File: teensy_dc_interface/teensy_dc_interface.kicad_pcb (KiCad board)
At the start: 2 copper layers, 125 parts, among them J1 3.5mm_Mono_Switched_SymSmall_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, J2 3.5mm_Mono_Switched_SymSmall_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, J3 3.5mm_Mono_Switched_SymSmall_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, J4 3.5mm_Mono_Switched_SymSmall_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, J5 3.5mm_Mono_Switched_SymSmall_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, J6 3.5mm_Mono_Switched_SymSmall_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, J7 3.5mm_Mono_Switched_SymSmall_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, J8 3.5mm_Mono_Switched_SymSmall_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, U1 AK4458VN, U2 Teensy4.0, U3 AP65211A, U4 AP62200TWU-7, U5 NE5532, U6 NE5532, U7 NE5532, U8 NE5532

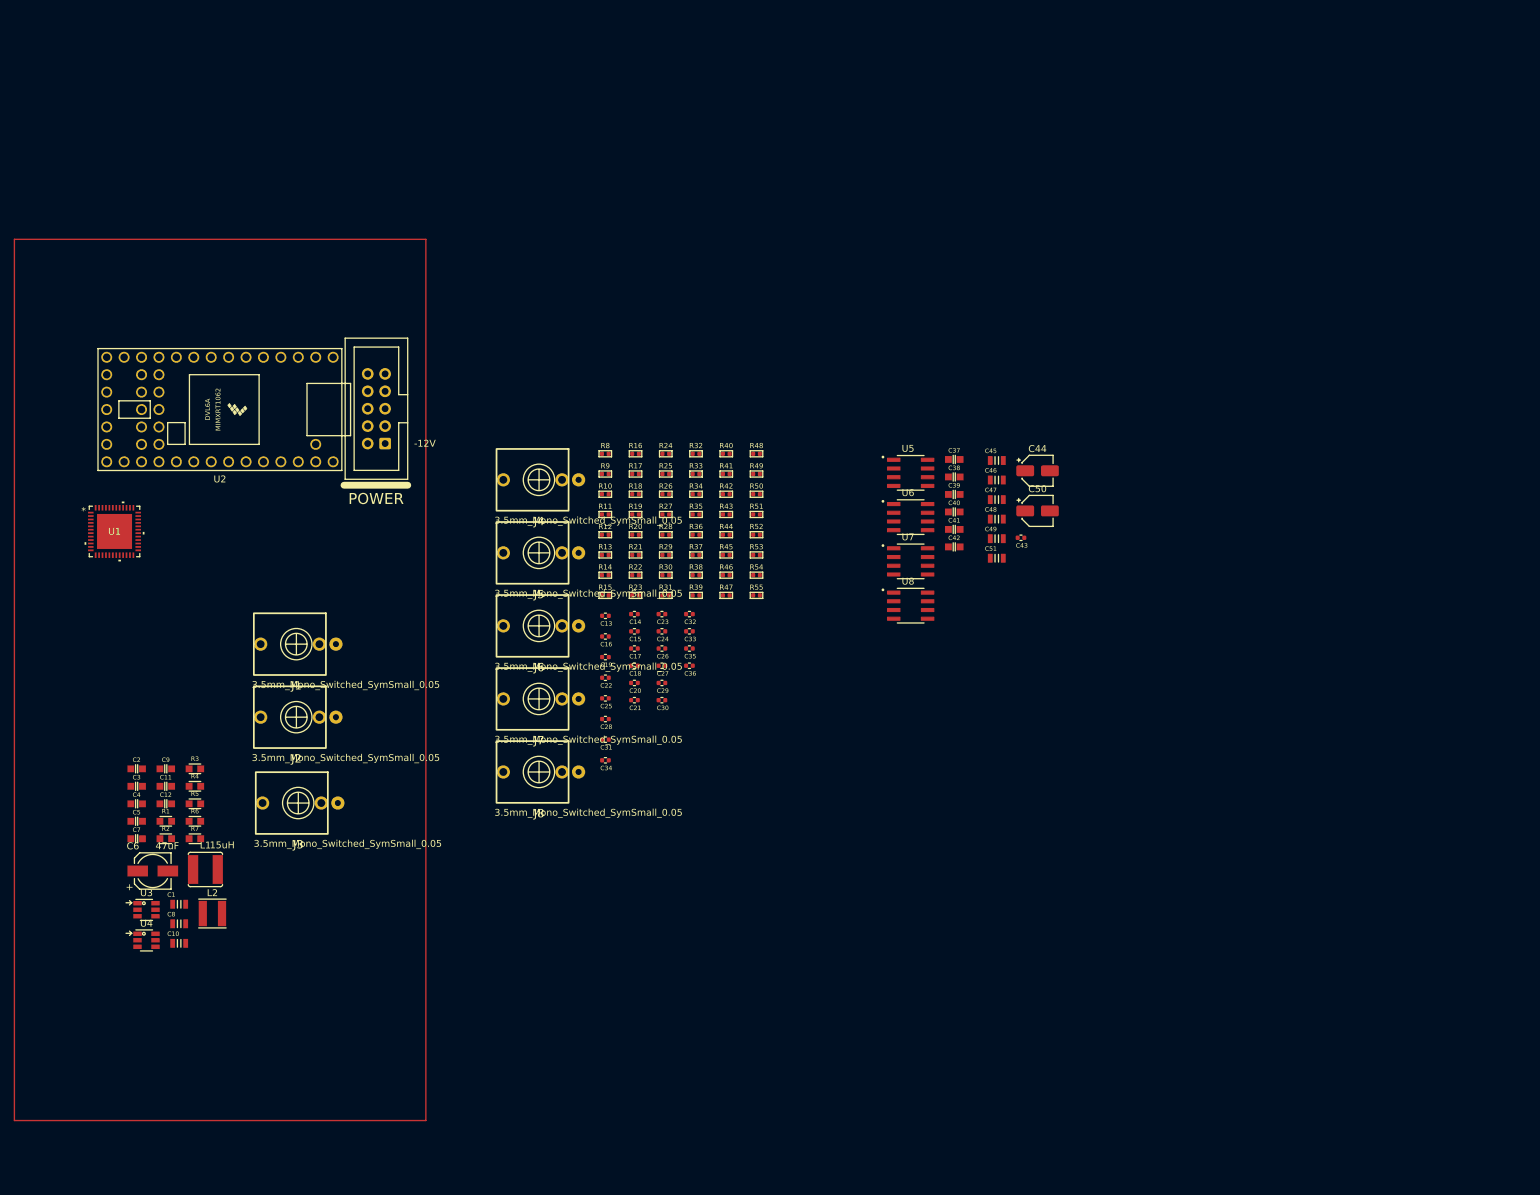
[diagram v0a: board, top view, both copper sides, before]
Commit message: teensy to dac connections
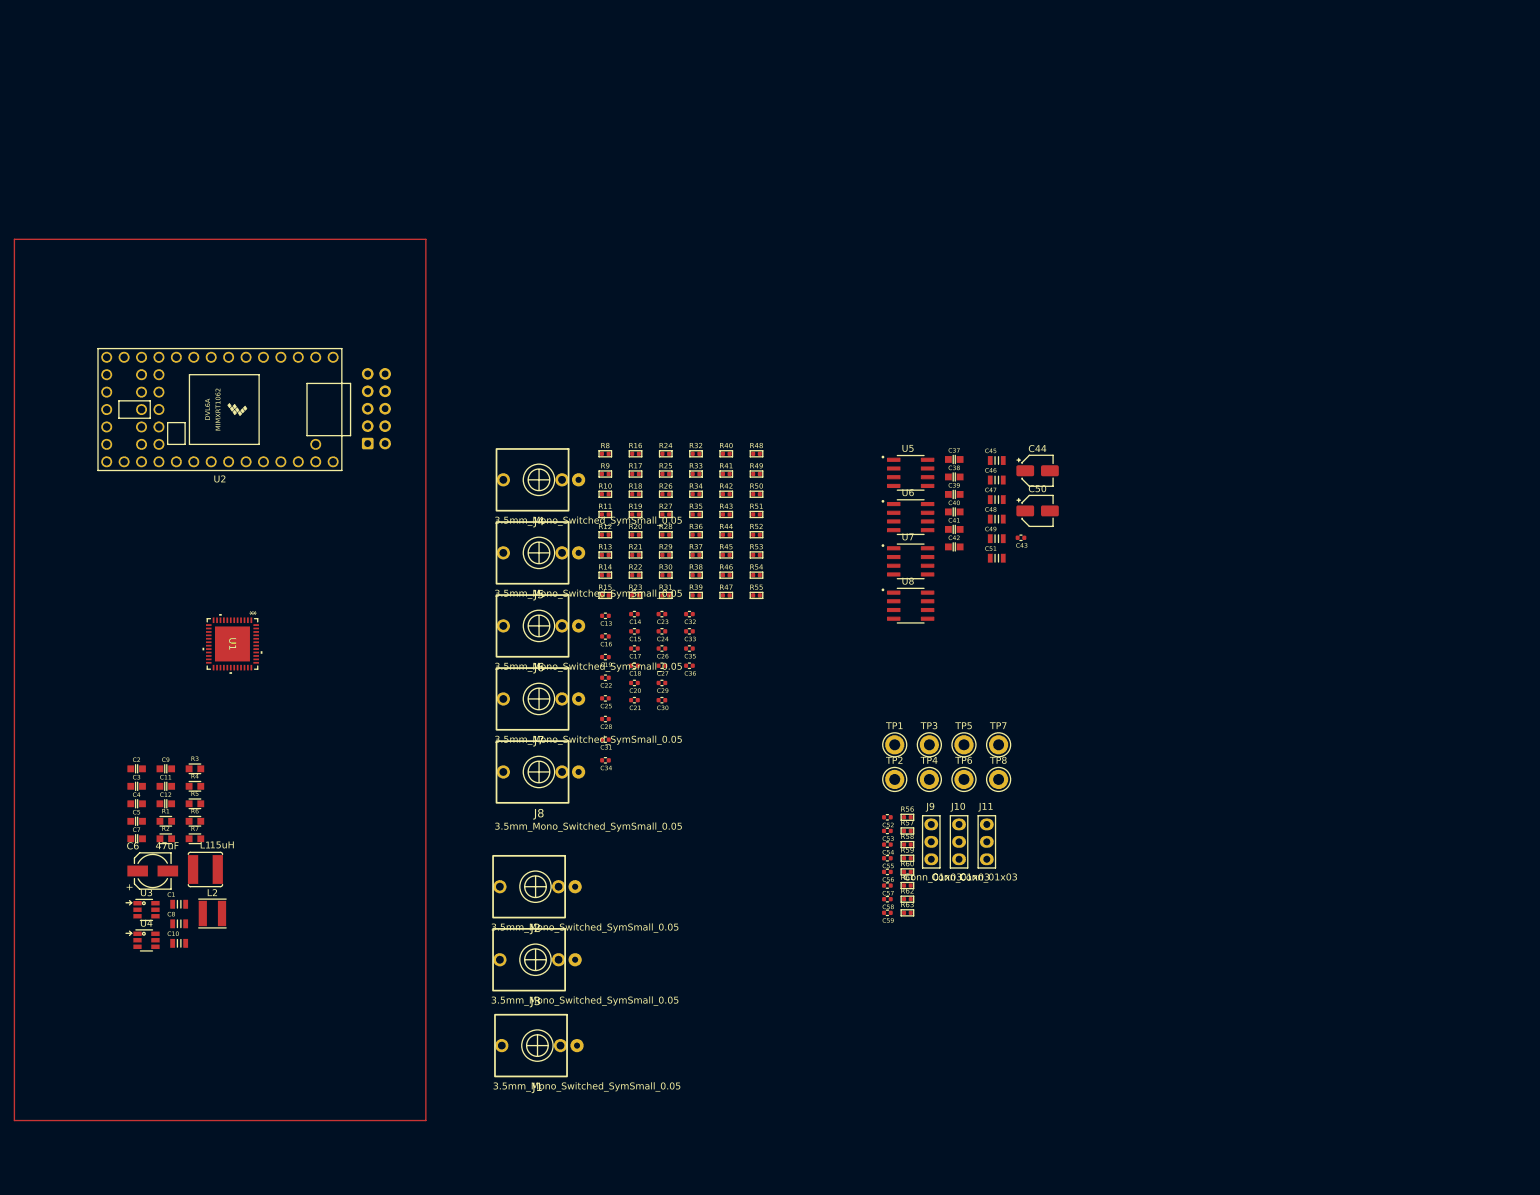
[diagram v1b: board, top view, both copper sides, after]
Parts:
- added C52: 220pF_0402_50V, 4ms_Capacitor:C_0402, F.Cu at (157.3, 104.3)
- added C53: 220pF_0402_50V, 4ms_Capacitor:C_0402, F.Cu at (157.3, 106.3)
- added C54: 220pF_0402_50V, 4ms_Capacitor:C_0402, F.Cu at (157.3, 108.3)
- added C55: 220pF_0402_50V, 4ms_Capacitor:C_0402, F.Cu at (157.3, 110.2)
- added C56: 220pF_0402_50V, 4ms_Capacitor:C_0402, F.Cu at (157.3, 112.2)
- added C57: 220pF_0402_50V, 4ms_Capacitor:C_0402, F.Cu at (157.3, 114.2)
- added C58: 220pF_0402_50V, 4ms_Capacitor:C_0402, F.Cu at (157.3, 116.2)
- added C59: 220pF_0402_50V, 4ms_Capacitor:C_0402, F.Cu at (157.3, 118.2)
- added J10: Conn_01x03, 4ms_Connector:Pins_1x03_2.54mm_TH, F.Cu at (167.8, 107.9)
- added J11: Conn_01x03, 4ms_Connector:Pins_1x03_2.54mm_TH, F.Cu at (171.8, 107.9)
- added J9: Conn_01x03, 4ms_Connector:Pins_1x03_2.54mm_TH, F.Cu at (163.7, 107.9)
- added R56: 10R_0402, 4ms_Resistor:R_0402, F.Cu at (160.2, 104.3)
- added R57: 10R_0402, 4ms_Resistor:R_0402, F.Cu at (160.2, 106.3)
- added R58: 10R_0402, 4ms_Resistor:R_0402, F.Cu at (160.2, 108.3)
- added R59: 10R_0402, 4ms_Resistor:R_0402, F.Cu at (160.2, 110.2)
- added R60: 10R_0402, 4ms_Resistor:R_0402, F.Cu at (160.2, 112.2)
- added R61: 10R_0402, 4ms_Resistor:R_0402, F.Cu at (160.2, 114.2)
- added R62: 10R_0402, 4ms_Resistor:R_0402, F.Cu at (160.2, 116.2)
- added R63: 10R_0402, 4ms_Resistor:R_0402, F.Cu at (160.2, 118.2)
- added TP1: TestPoint_Small, TestPoint:TestPoint_Keystone_5005-5009_Compact, F.Cu at (158.4, 93.7)
- added TP2: TestPoint_Small, TestPoint:TestPoint_Keystone_5005-5009_Compact, F.Cu at (158.4, 98.8)
- added TP3: TestPoint_Small, TestPoint:TestPoint_Keystone_5005-5009_Compact, F.Cu at (163.4, 93.7)
- added TP4: TestPoint_Small, TestPoint:TestPoint_Keystone_5005-5009_Compact, F.Cu at (163.4, 98.8)
- added TP5: TestPoint_Small, TestPoint:TestPoint_Keystone_5005-5009_Compact, F.Cu at (168.5, 93.7)
- added TP6: TestPoint_Small, TestPoint:TestPoint_Keystone_5005-5009_Compact, F.Cu at (168.5, 98.8)
- added TP7: TestPoint_Small, TestPoint:TestPoint_Keystone_5005-5009_Compact, F.Cu at (173.5, 93.7)
- added TP8: TestPoint_Small, TestPoint:TestPoint_Keystone_5005-5009_Compact, F.Cu at (173.5, 98.8)
- H1: moved to B.Cu
- moved J1 68.3 mm to (106.3, 137.6)
- moved J2 42.8 mm to (106.0, 114.4)
- moved J3 41.5 mm to (106.0, 125.0)
- moved U1 23.8 mm to (61.8, 79.0), turned to -90 degrees
- turned H1 to 180 degrees
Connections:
- C10 pad 2: AVSS -> DVSS
- C11 pad 2: AVSS -> DVSS
- C12 pad 2: AVSS -> DVSS
- C43 pad 1: AVSS -> DVSS
- C44 pad 2: AVSS -> DVSS
- C45 pad 1: AVSS -> DVSS
- C7 pad 2: AVSS -> DVSS
- C8 pad 2: AVSS -> DVSS
- H1 pad 3: AVSS -> DVSS
- H1 pad 5: AVSS -> DVSS
- H1 pad 7: AVSS -> DVSS
- R7 pad 2: AVSS -> DVSS
- U1 pad 10: DSDR4 -> DVSS
- U1 pad 12: AVSS -> DVSS
- U1 pad 15: AVSS -> DVSS
- U1 pad 16: AVSS -> DVSS
- U1 pad 46: AVSS -> DVSS
- U1 pad 49: EPAD -> unconnected-(U1-EPAD-Pad49)
- U1 pad 8: DSDR3 -> DVSS
- U1 pad 9: DSDL4 -> DVSS
- U2 pad 1: AVSS -> DVSS
- U2 pad 11: unconnected-(U2-9_OUT1C-Pad11) -> 9_OUT1C
- U2 pad 17: AVSS -> unconnected-(U2-GND-Pad17)
- U2 pad 24: unconnected-(U2-17_A3_TX4_SDA1-Pad24) -> PDN
- U2 pad 25: unconnected-(U2-18_A4_SDA0-Pad25) -> SDA/CDTI/TDM0
- U2 pad 26: unconnected-(U2-19_A5_SCL0-Pad26) -> SCL/CCLK/TDM1
- U2 pad 27: unconnected-(U2-20_A6_TX5_LRCLK1-Pad27) -> LRCK/DSDL1
- U2 pad 28: unconnected-(U2-21_A7_RX5_BCLK1-Pad28) -> BICK/DCLK
- U2 pad 30: unconnected-(U2-23_A9_CRX1_MCLK1-Pad30) -> MCLK
- U2 pad 32: AVSS -> DVSS
- U2 pad 43: unconnected-(U2-32_OUT1B-Pad43) -> 32_OUT1B
- U2 pad 8: unconnected-(U2-6_OUT1D-Pad8) -> 6_OUT1D
- U2 pad 9: unconnected-(U2-7_RX2_OUT1A-Pad9) -> SDTI1/DSDR1
- U4 pad 1: AVSS -> DVSS

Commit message: Created first set of DAC outputs layout
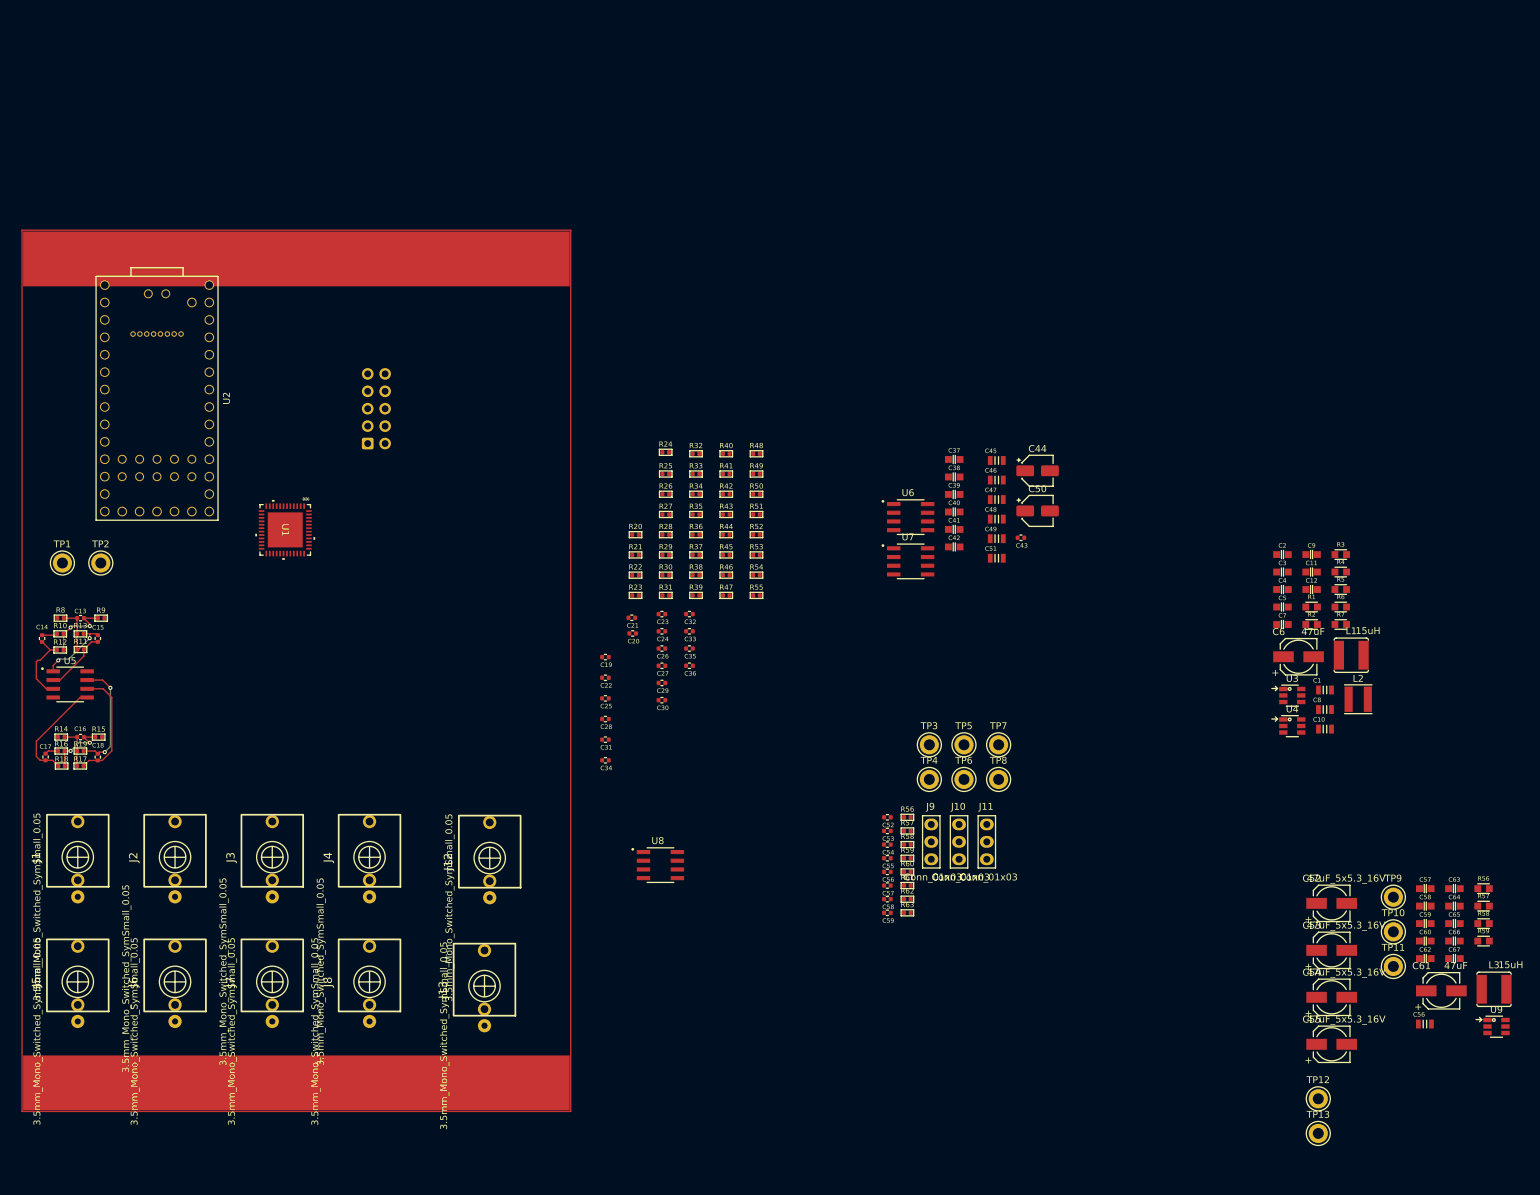
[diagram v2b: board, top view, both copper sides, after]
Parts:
- added ?: , , F.Cu at (71.1, 143.0)
- added C52: 47uF_5x5.3_16V, 4ms_Capacitor:CP_Elec_5x5.3, F.Cu at (222.1, 116.8)
- added C53: 47uF_5x5.3_16V, 4ms_Capacitor:CP_Elec_5x5.3, F.Cu at (222.1, 123.7)
- added C54: 47uF_5x5.3_16V, 4ms_Capacitor:CP_Elec_5x5.3, F.Cu at (222.1, 130.5)
- added C55: 47uF_5x5.3_16V, 4ms_Capacitor:CP_Elec_5x5.3, F.Cu at (222.1, 137.4)
- added C56: 22uF, 4ms_Capacitor:C_0805, F.Cu at (235.7, 134.4)
- added C57: 0.1uF, 4ms_Capacitor:C_0603, F.Cu at (235.7, 114.7)
- added C58: 47pF, 4ms_Capacitor:C_0603, F.Cu at (235.7, 117.2)
- added C59: 22uF, 4ms_Capacitor:C_0603, F.Cu at (235.7, 119.8)
- added C60: 10uF, 4ms_Capacitor:C_0603, F.Cu at (235.7, 122.3)
- added C61: 47uF, 4ms_Capacitor:CP_Elec_5x5.3, F.Cu at (238.1, 129.6)
- added C62: 0.1uF_0603_16V, 4ms_Capacitor:C_0603, F.Cu at (235.7, 124.9)
- added C63: 0.1uF_0603_16V, 4ms_Capacitor:C_0603, F.Cu at (240.0, 114.7)
- added C64: 0.1uF_0603_16V, 4ms_Capacitor:C_0603, F.Cu at (240.0, 117.2)
- added C65: 0.1uF_0603_16V, 4ms_Capacitor:C_0603, F.Cu at (240.0, 119.8)
- added C66: 0.1uF_0603_16V, 4ms_Capacitor:C_0603, F.Cu at (240.0, 122.3)
- added C67: 0.1uF_0603_16V, 4ms_Capacitor:C_0603, F.Cu at (240.0, 124.9)
- added J12: 3.5mm_Mono_Switched_SymSmall_0.05, 4ms_Jack:EighthInch_PJ398SM, F.Cu at (99.3, 110.2)
- added J13: 3.5mm_Mono_Switched_SymSmall_0.05, 4ms_Jack:EighthInch_PJ398SM, F.Cu at (98.6, 128.9)
- added L3: 15uH, 4ms_Inductor:COIL_5040, F.Cu at (245.8, 129.4)
- added R56: 100k, 4ms_Resistor:R_0603, F.Cu at (244.2, 114.7)
- added R57: 75k, 4ms_Resistor:R_0603, F.Cu at (244.2, 117.2)
- added R58: 40.2k, 4ms_Resistor:R_0603, F.Cu at (244.2, 119.8)
- added R59: 7.68k, 4ms_Resistor:R_0603, F.Cu at (244.2, 122.3)
- added REF**: Rail_Connection_16HP, 4ms_Faceplate:Rail_Connection_16HP, F.Cu at (71.1, 22.9)
- added TP10: TestPoint_Small, TestPoint:TestPoint_Keystone_5005-5009_Compact, F.Cu at (231.1, 121.0)
- added TP11: TestPoint_Small, TestPoint:TestPoint_Keystone_5005-5009_Compact, F.Cu at (231.1, 126.0)
- added TP12: TestPoint_Small, TestPoint:TestPoint_Keystone_5005-5009_Compact, F.Cu at (220.1, 145.3)
- added TP13: TestPoint_Small, TestPoint:TestPoint_Keystone_5005-5009_Compact, F.Cu at (220.1, 150.4)
- added TP9: TestPoint_Small, TestPoint:TestPoint_Keystone_5005-5009_Compact, F.Cu at (231.1, 115.9)
- added U9: AP65211A, 4ms_Package_SOT:TSOT-23-6, F.Cu at (246.1, 134.8)
- U2: footprint teensy:Teensy40 -> teensy:Teensy40_SMT
- moved C1 170.0 mm to (221.1, 85.7)
- moved C10 170.0 mm to (221.1, 91.4)
- moved C11 170.0 mm to (219.2, 68.5)
- moved C12 170.0 mm to (219.2, 71.1)
- moved C2 170.0 mm to (214.9, 66.0)
- moved C3 170.0 mm to (214.9, 68.5)
- moved C4 170.0 mm to (214.9, 71.1)
- moved C5 170.0 mm to (214.9, 73.6)
- moved C6 170.0 mm to (217.3, 80.9)
- moved C7 170.0 mm to (214.9, 76.2)
- moved C8 170.0 mm to (221.1, 88.6)
- moved C9 170.0 mm to (219.2, 66.0)
- moved L1 170.0 mm to (224.9, 80.6)
- moved L2 170.0 mm to (226.0, 87.1)
- moved R1 170.0 mm to (219.2, 73.6)
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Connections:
- U1 pad 34: AVSS -> AVDD
- U1 pad 35: AVDD -> AVSS
- U1 pad 40: AVSS -> AVDD
- U1 pad 41: AVDD -> AVSS
- U2 pad 17: unconnected-(U2-GND-Pad17) -> DVSS
- U2 pad 22: unconnected-(U2-15_A1_RX3_SPDIF_IN-Pad22) -> PDN
- U2 pad 23: unconnected-(U2-16_A2_RX4_SCL1-Pad23) -> ADC2
- U2 pad 24: PDN -> ADC3
- U2 pad 33: TVDD -> Teensy_5V
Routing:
- net OP2_NEG: track 0.00 -> 16.9 mm
- net OP2_OUT: track 0.00 -> 16.9 mm, vias 0 -> 2
- net OP2_POS: track 0.00 -> 16.0 mm
- net OP1_POS: track 0.00 -> 10.9 mm
- net OP1_OUT: track 0.00 -> 10.6 mm, vias 0 -> 2
- net Net-(C13-Pad2): track 0.00 -> 10.2 mm, vias 0 -> 2
- net OP1_NEG: track 0.00 -> 9.38 mm
- net Net-(C16-Pad2): track 0.00 -> 9.28 mm, vias 0 -> 2
- net Net-(C13-Pad1): track 0.00 -> 6.54 mm
- net Net-(C16-Pad1): track 0.00 -> 6.08 mm
- net AVSS: track 0.00 -> 4.20 mm
